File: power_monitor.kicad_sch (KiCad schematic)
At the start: 31 parts, among them J11 Conn_01x02_Male, J9 Conn_01x03_Male, U2 CJ431, U3 TMP23X, U4 ACS712xLCTR-20A, U5 ADC108S022CIMTX

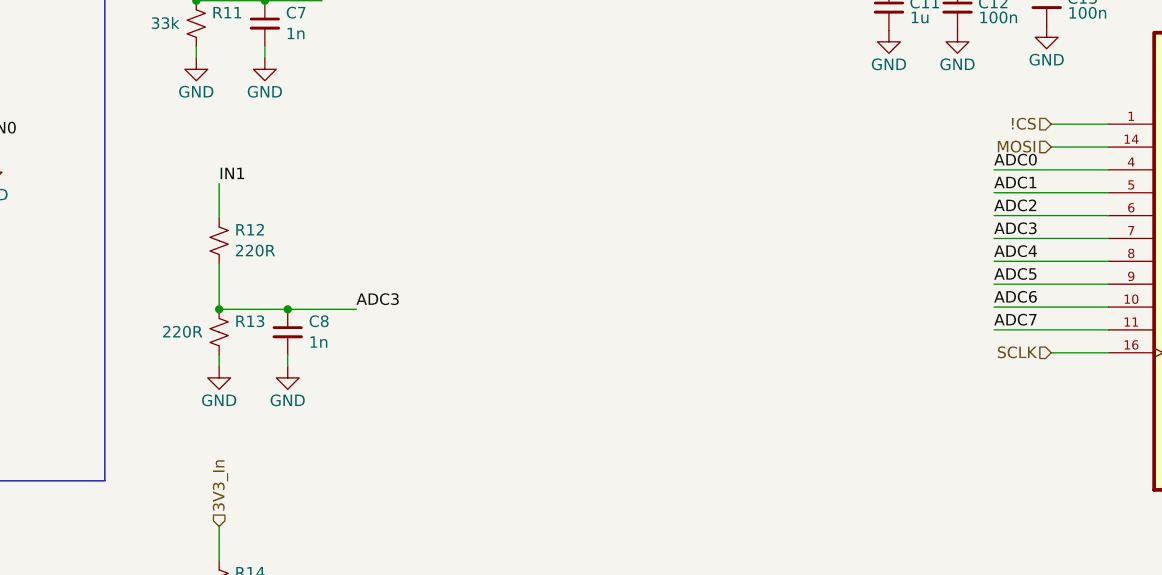
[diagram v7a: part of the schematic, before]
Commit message: Updated power circuit. Fixed U1 footprint.
-Dropped ADC1 and ADC3 connections
-Dropped IN1 branch
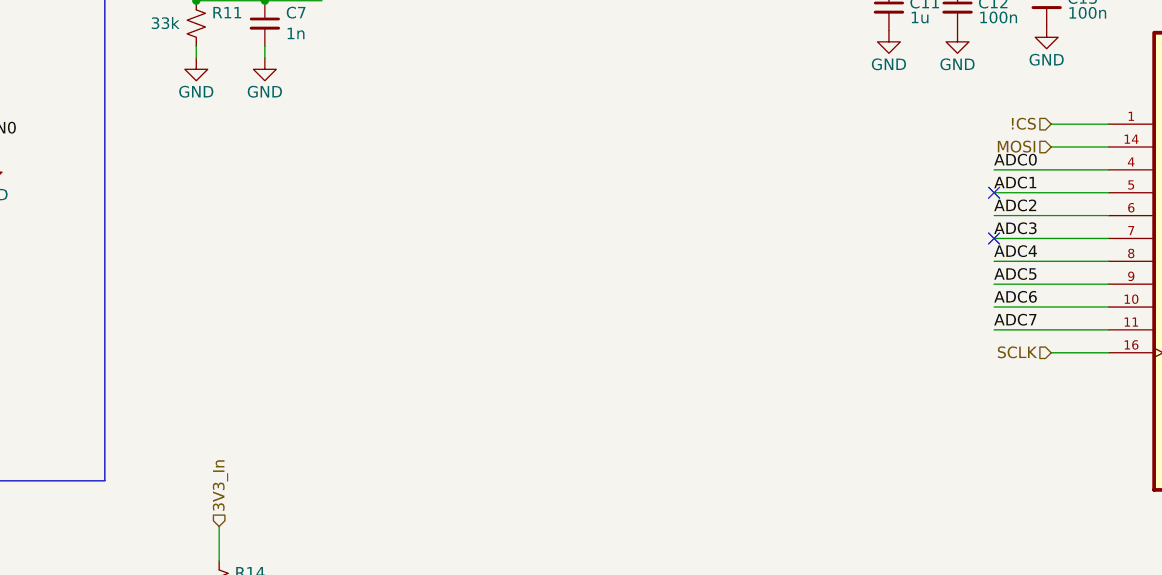
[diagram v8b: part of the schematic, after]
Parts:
- removed C8: 1n, Capacitor_SMD:C_0402_1005Metric, symbol Device:C_Small
- removed R12, R13: 220R, Resistor_SMD:R_0402_1005Metric, symbol Device:R_Small_US
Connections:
- no-connect marks 2 -> 4
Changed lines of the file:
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@@
     (comment 2 "@reference Pi_ADC/Justin Pead")
-  )
-  (junction (at 118.11 90.17) (diameter 0) (color 0 0 0 0)
-  )
-  (junction (at 125.73 90.17) (diameter 0) (color 0 0 0 0)
   )
   (junction (at 118.11 128.27) (diameter 0) (color 0 0 0 0)
@@
   (no_connect (at 42.418 145.288))
   (no_connect (at 37.338 145.288))
+  (no_connect (at 204.216 82.296))
+  (no_connect (at 204.216 77.216))
   (wire (pts (xy 102.87 45.72) (xy 99.06 45.72))
     (stroke (width 0) (type default))
@@
     (stroke (width 0) (type default))
   )
-  (wire (pts (xy 125.73 90.17) (xy 133.35 90.17))
-    (stroke (width 0) (type default))
-  )
   (wire (pts (xy 39.37 176.53) (xy 39.37 175.26))
     (stroke (width 0) (type default))
@@
     (stroke (width 0) (type default))
   )
-  (wire (pts (xy 118.11 80.01) (xy 118.11 76.2))
-    (stroke (width 0) (type default))
-  )
   (wire (pts (xy 216.916 82.296) (xy 204.216 82.296))
     (stroke (width 0) (type default))
@@
     (stroke (width 0) (type default))
   )
-  (wire (pts (xy 118.11 95.25) (xy 118.11 96.52))
-    (stroke (width 0) (type default))
-  )
   (wire (pts (xy 34.29 68.58) (xy 34.29 71.12))
     (stroke (width 0) (type default))
@@
     (stroke (width 0) (type default))
   )
-  (wire (pts (xy 118.11 90.17) (xy 125.73 90.17))
-    (stroke (width 0) (type default))
-  )
   (wire (pts (xy 124.46 144.78) (xy 124.46 156.21))
     (stroke (width 0) (type default))
@@
     (stroke (width 0) (type default))
   )
-  (wire (pts (xy 125.73 95.25) (xy 125.73 96.52))
-    (stroke (width 0) (type default))
-  )
   (wire (pts (xy 41.91 55.88) (xy 41.91 54.61))
-    (stroke (width 0) (type default))
-  )
-  (wire (pts (xy 118.11 90.17) (xy 118.11 85.09))
     (stroke (width 0) (type default))
   )
@@
     (effects (font (size 1.27 1.27)) (justify left bottom))
   )
-  (label "IN1" (at 118.11 76.2 0) (fields_autoplaced)
-    (effects (font (size 1.27 1.27)) (justify left bottom))
-  )
   (label "ADC5" (at 204.216 87.376 0) (fields_autoplaced)
-    (effects (font (size 1.27 1.27)) (justify left bottom))
-  )
-  (label "ADC3" (at 133.35 90.17 0) (fields_autoplaced)
     (effects (font (size 1.27 1.27)) (justify left bottom))
   )
@@
     )
   )
-  (symbol (lib_id "Device:R_Small_US") (at 118.11 92.71 0) (unit 1)
-    (in_bom yes) (on_board yes) (dnp no)
-    (property "Reference" "R13" (at 119.8372 91.5416 0)
-      (effects (font (size 1.27 1.27)) (justify left))
-    )
-    (property "Value" "220R" (at 111.76 92.71 0)
-      (effects (font (size 1.27 1.27)) (justify left))
-    )
-    (property "Footprint" "Resistor_SMD:R_0402_1005Metric" (at 118.11 92.71 0)
-      (effects (font (size 1.27 1.27)) hide)
-    )
-    (property "Datasheet" "~" (at 118.11 92.71 0)
-      (effects (font (size 1.27 1.27)) hide)
-    )
-    (property "Populate" "1" (at 118.11 92.71 0)
-      (effects (font (size 1.27 1.27)) hide)
-    )
-    (property "Extended" "0" (at 118.11 92.71 0)
-      (effects (font (size 1.27 1.27)) hide)
-    )
-    (property "LCSC" "C25091" (at 118.11 92.71 0)
-      (effects (font (size 1.27 1.27)) hide)
-    )
-    (pin "1")
-    (pin "2")
-    (instances
-      (project "Pi HAT"
-        (path "/48f827a8-6e22-4a2e-abdc-c2a03098d883/715798e8-ada1-4b31-bdfe-4378c151d2b8"
-          (reference "R13") (unit 1)
-        )
-      )
-    )
-  )
-  (symbol (lib_id "Device:R_Small_US") (at 118.11 82.55 0) (unit 1)
-    (in_bom yes) (on_board yes) (dnp no)
-    (property "Reference" "R12" (at 119.8372 81.3816 0)
-      (effects (font (size 1.27 1.27)) (justify left))
-    )
-    (property "Value" "220R" (at 119.8372 83.693 0)
-      (effects (font (size 1.27 1.27)) (justify left))
-    )
-    (property "Footprint" "Resistor_SMD:R_0402_1005Metric" (at 118.11 82.55 0)
-      (effects (font (size 1.27 1.27)) hide)
-    )
-    (property "Datasheet" "~" (at 118.11 82.55 0)
-      (effects (font (size 1.27 1.27)) hide)
-    )
-    (property "Populate" "1" (at 118.11 82.55 0)
-      (effects (font (size 1.27 1.27)) hide)
-    )
-    (property "Extended" "0" (at 118.11 82.55 0)
-      (effects (font (size 1.27 1.27)) hide)
-    )
-    (property "LCSC" "C25091" (at 118.11 82.55 0)
-      (effects (font (size 1.27 1.27)) hide)
-    )
-    (pin "1")
-    (pin "2")
-    (instances
-      (project "Pi HAT"
-        (path "/48f827a8-6e22-4a2e-abdc-c2a03098d883/715798e8-ada1-4b31-bdfe-4378c151d2b8"
-          (reference "R12") (unit 1)
-        )
-      )
-    )
-  )
-  (symbol (lib_id "Device:C_Small") (at 125.73 92.71 0) (unit 1)
-    (in_bom yes) (on_board yes) (dnp no)
-    (property "Reference" "C8" (at 128.0668 91.5416 0)
-      (effects (font (size 1.27 1.27)) (justify left))
-    )
-    (property "Value" "1n" (at 128.0668 93.853 0)
-      (effects (font (size 1.27 1.27)) (justify left))
-    )
-    (property "Footprint" "Capacitor_SMD:C_0402_1005Metric" (at 125.73 92.71 0)
-      (effects (font (size 1.27 1.27)) hide)
-    )
-    (property "Datasheet" "~" (at 125.73 92.71 0)
-      (effects (font (size 1.27 1.27)) hide)
-    )
-    (property "Extended" "0" (at 125.73 92.71 0)
-      (effects (font (size 1.27 1.27)) hide)
-    )
-    (property "LCSC" "C1523" (at 125.73 92.71 0)
-      (effects (font (size 1.27 1.27)) hide)
-    )
-    (property "Populate" "1" (at 125.73 92.71 0)
-      (effects (font (size 1.27 1.27)) hide)
-    )
-    (property "Price" "0.001" (at 125.73 92.71 0)
-      (effects (font (size 1.27 1.27)) hide)
-    )
-    (pin "1")
-    (pin "2")
-    (instances
-      (project "Pi HAT"
-        (path "/48f827a8-6e22-4a2e-abdc-c2a03098d883/715798e8-ada1-4b31-bdfe-4378c151d2b8"
-          (reference "C8") (unit 1)
-        )
-      )
-    )
-  )
   (symbol (lib_id "Connector:Conn_01x03_Pin") (at 87.63 71.12 0) (unit 1)
     (in_bom yes) (on_board yes) (dnp no)
@@
         (path "/48f827a8-6e22-4a2e-abdc-c2a03098d883/715798e8-ada1-4b31-bdfe-4378c151d2b8"
           (reference "#PWR045") (unit 1)
-        )
-      )
-    )
-  )
-  (symbol (lib_id "power:GND") (at 118.11 96.52 0) (unit 1)
-    (in_bom yes) (on_board yes) (dnp no)
-    (property "Reference" "#PWR07" (at 118.11 102.87 0)
-      (effects (font (size 1.27 1.27)) hide)
-    )
-    (property "Value" "GND" (at 118.11 100.33 0)
-      (effects (font (size 1.27 1.27)))
-    )
-    (property "Footprint" "" (at 118.11 96.52 0)
-      (effects (font (size 1.27 1.27)) hide)
-    )
-    (property "Datasheet" "" (at 118.11 96.52 0)
-      (effects (font (size 1.27 1.27)) hide)
-    )
-    (pin "1")
-    (instances
-      (project "Pi HAT"
-        (path "/48f827a8-6e22-4a2e-abdc-c2a03098d883"
-          (reference "#PWR07") (unit 1)
-        )
-        (path "/48f827a8-6e22-4a2e-abdc-c2a03098d883/715798e8-ada1-4b31-bdfe-4378c151d2b8"
-          (reference "#PWR040") (unit 1)
         )
       )
@@
         )
       )
-    )
-  )
-  (symbol (lib_id "power:GND") (at 125.73 96.52 0) (unit 1)
-    (in_bom yes) (on_board yes) (dnp no)
-    (property "Reference" "#PWR07" (at 125.73 102.87 0)
-      (effects (font (size 1.27 1.27)) hide)
-    )
-    (property "Value" "GND" (at 125.73 100.33 0)
-      (effects (font (size 1.27 1.27)))
-    )
-    (property "Footprint" "" (at 125.73 96.52 0)
-      (effects (font (size 1.27 1.27)) hide)
-    )
-    (property "Datasheet" "" (at 125.73 96.52 0)
-      (effects (font (size 1.27 1.27)) hide)
-    )
-    (pin "1")
-    (instances
-      (project "Pi HAT"
-        (path "/48f827a8-6e22-4a2e-abdc-c2a03098d883"
-          (reference "#PWR07") (unit 1)
-        )
-        (path "/48f827a8-6e22-4a2e-abdc-c2a03098d883/715798e8-ada1-4b31-bdfe-4378c151d2b8"
-          (reference "#PWR041") (unit 1)
-        )
-      )
